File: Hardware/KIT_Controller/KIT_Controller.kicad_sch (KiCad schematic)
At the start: 1 part

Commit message: Satisfy constraints
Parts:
- added C1: 4.7uf, Capacitor_SMD:C_0805_2012Metric, symbol Device:C_Small
- added JP1: SolderJumper_2_Open, Jumper:SolderJumper-2_P1.3mm_Open_TrianglePad1.0x1.5mm, symbol Jumper:SolderJumper_2_Open
- gave numbers to parts that had none: 1
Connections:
- net at U1.2 (VOUT): now also C1.1
- net GND: now reaches U1.3 (GND)
- net GND: now also C1.2
- net at U1.4 (OSC): now also JP1.1 (A)
- net +3.3V: now reaches U1.9 (VCC)
- net +3.3V: now also JP1.2 (B)
- no-connect marks 0 -> 5
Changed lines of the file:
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@@
 (kicad_sch (version 20211123) (generator eeschema)
   (paper "A4")
+  (junction (at 224.79 114.3) (diameter 0) (color 0 0 0 0)
+  )
+  (junction (at 226.06 76.2) (diameter 0) (color 0 0 0 0)
+  )
+  (no_connect (at 212.09 97.155))
+  (no_connect (at 212.09 92.075))
+  (no_connect (at 212.09 94.615))
+  (no_connect (at 212.09 88.265))
+  (no_connect (at 212.09 99.695))
+  (wire (pts (xy 221.615 76.2) (xy 226.06 76.2))
+    (stroke (width 0) (type default) (color 0 0 0 0))
+  )
+  (wire (pts (xy 212.09 84.455) (xy 209.55 84.455))
+    (stroke (width 0) (type default) (color 0 0 0 0))
+  )
+  (wire (pts (xy 209.55 76.2) (xy 213.995 76.2))
+    (stroke (width 0) (type default) (color 0 0 0 0))
+  )
+  (wire (pts (xy 226.06 76.2) (xy 226.06 76.835))
+    (stroke (width 0) (type default) (color 0 0 0 0))
+  )
+  (wire (pts (xy 209.55 84.455) (xy 209.55 76.2))
+    (stroke (width 0) (type default) (color 0 0 0 0))
+  )
+  (wire (pts (xy 227.33 107.315) (xy 227.33 108.585))
+    (stroke (width 0) (type default) (color 0 0 0 0))
+  )
+  (wire (pts (xy 226.06 74.93) (xy 226.06 76.2))
+    (stroke (width 0) (type default) (color 0 0 0 0))
+  )
+  (wire (pts (xy 227.33 114.3) (xy 224.79 114.3))
+    (stroke (width 0) (type default) (color 0 0 0 0))
+  )
+  (wire (pts (xy 224.79 114.3) (xy 224.79 116.205))
+    (stroke (width 0) (type default) (color 0 0 0 0))
+  )
+  (wire (pts (xy 224.79 107.315) (xy 224.79 114.3))
+    (stroke (width 0) (type default) (color 0 0 0 0))
+  )
+  (wire (pts (xy 227.33 113.665) (xy 227.33 114.3))
+    (stroke (width 0) (type default) (color 0 0 0 0))
+  )
+  (symbol (lib_id "Jumper:SolderJumper_2_Open") (at 217.805 76.2 0) (unit 1)
+    (in_bom yes) (on_board yes)
+    (property "Reference" "JP1" (id 0) (at 217.805 73.66 0))
+    (property "Value" "SolderJumper_2_Open" (id 1) (at 217.805 72.39 0)
+      (effects (font (size 1.27 1.27)) hide)
+    )
+    (property "Footprint" "Jumper:SolderJumper-2_P1.3mm_Open_TrianglePad1.0x1.5mm" (id 2) (at 217.805 76.2 0)
+      (effects (font (size 1.27 1.27)) hide)
+    )
+    (property "Datasheet" "~" (id 3) (at 217.805 76.2 0)
+      (effects (font (size 1.27 1.27)) hide)
+    )
+    (pin "1")
+    (pin "2")
+  )
+  (symbol (lib_id "power:+3.3V") (at 226.06 74.93 0) (unit 1)
+    (in_bom yes) (on_board yes) (fields_autoplaced)
+    (property "Reference" "#PWR02" (id 0) (at 226.06 78.74 0)
+      (effects (font (size 1.27 1.27)) hide)
+    )
+    (property "Value" "+3.3V" (id 1) (at 226.06 69.85 0))
+    (property "Footprint" "" (id 2) (at 226.06 74.93 0)
+      (effects (font (size 1.27 1.27)) hide)
+    )
+    (property "Datasheet" "" (id 3) (at 226.06 74.93 0)
+      (effects (font (size 1.27 1.27)) hide)
+    )
+    (pin "1")
+  )
+  (symbol (lib_id "power:PWR_FLAG") (at 224.79 114.3 90) (unit 1)
+    (in_bom yes) (on_board yes) (fields_autoplaced)
+    (property "Reference" "#FLG0101" (id 0) (at 222.885 114.3 0)
+      (effects (font (size 1.27 1.27)) hide)
+    )
+    (property "Value" "PWR_FLAG" (id 1) (at 223.52 110.49 90))
+    (property "Footprint" "" (id 2) (at 224.79 114.3 0)
+      (effects (font (size 1.27 1.27)) hide)
+    )
+    (property "Datasheet" "~" (id 3) (at 224.79 114.3 0)
+      (effects (font (size 1.27 1.27)) hide)
+    )
+    (pin "1")
+  )
   (symbol (lib_id "nokia_5110-3310_lcd:Nokia_5110_LCD") (at 223.52 93.345 0) (unit 1)
     (in_bom yes) (on_board yes) (fields_autoplaced)
-    (property "Reference" "U?" (id 0) (at 231.14 90.805 0)
+    (property "Reference" "U1" (id 0) (at 231.14 90.805 0)
       (effects (font (size 1.524 1.524)) (justify left))
     )
@@
     (pin "9")
   )
+  (symbol (lib_id "Device:C_Small") (at 227.33 111.125 0) (unit 1)
+    (in_bom yes) (on_board yes) (fields_autoplaced)
+    (property "Reference" "C1" (id 0) (at 230.505 109.8612 0)
+      (effects (font (size 1.27 1.27)) (justify left))
+    )
+    (property "Value" "4.7uf" (id 1) (at 230.505 112.4012 0)
+      (effects (font (size 1.27 1.27)) (justify left))
+    )
+    (property "Footprint" "Capacitor_SMD:C_0805_2012Metric" (id 2) (at 227.33 111.125 0)
+      (effects (font (size 1.27 1.27)) hide)
+    )
+    (property "Datasheet" "~" (id 3) (at 227.33 111.125 0)
+      (effects (font (size 1.27 1.27)) hide)
+    )
+    (pin "1")
+    (pin "2")
+  )
+  (symbol (lib_id "power:GND") (at 224.79 116.205 0) (unit 1)
+    (in_bom yes) (on_board yes) (fields_autoplaced)
+    (property "Reference" "#PWR01" (id 0) (at 224.79 122.555 0)
+      (effects (font (size 1.27 1.27)) hide)
+    )
+    (property "Value" "GND" (id 1) (at 224.79 121.285 0))
+    (property "Footprint" "" (id 2) (at 224.79 116.205 0)
+      (effects (font (size 1.27 1.27)) hide)
+    )
+    (property "Datasheet" "" (id 3) (at 224.79 116.205 0)
+      (effects (font (size 1.27 1.27)) hide)
+    )
+    (pin "1")
+  )
+  (symbol (lib_id "power:PWR_FLAG") (at 226.06 76.2 270) (unit 1)
+    (in_bom yes) (on_board yes) (fields_autoplaced)
+    (property "Reference" "#FLG0102" (id 0) (at 227.965 76.2 0)
+      (effects (font (size 1.27 1.27)) hide)
+    )
+    (property "Value" "PWR_FLAG" (id 1) (at 229.87 76.1999 90)
+      (effects (font (size 1.27 1.27)) (justify left))
+    )
+    (property "Footprint" "" (id 2) (at 226.06 76.2 0)
+      (effects (font (size 1.27 1.27)) hide)
+    )
+    (property "Datasheet" "~" (id 3) (at 226.06 76.2 0)
+      (effects (font (size 1.27 1.27)) hide)
+    )
+    (pin "1")
+  )
   (sheet_instances
     (path "/" (page "1"))
   )
   (symbol_instances
+    (path "/4eb8585d-c31d-4b73-92b2-292a151f185e"
+      (reference "#FLG0101") (unit 1) (value "PWR_FLAG") (footprint "")
+    )
+    (path "/ecdf7f93-19b9-4617-b0cd-e32253294f59"
+      (reference "#FLG0102") (unit 1) (value "PWR_FLAG") (footprint "")
+    )
+    (path "/846a239b-d6fe-40f8-ba97-eca7b90437c7"
+      (reference "#PWR01") (unit 1) (value "GND") (footprint "")
+    )
+    (path "/13f49aed-0c42-4453-bcb8-cd4e227fdfb5"
+      (reference "#PWR02") (unit 1) (value "+3.3V") (footprint "")
+    )
+    (path "/6ab78924-1dc0-46f4-aacc-52e33f151645"
+      (reference "C1") (unit 1) (value "4.7uf") (footprint "Capacitor_SMD:C_0805_2012Metric")
+    )
+    (path "/034c73e5-9967-4b8a-b103-11b25b0768f1"
+      (reference "JP1") (unit 1) (value "SolderJumper_2_Open") (footprint "Jumper:SolderJumper-2_P1.3mm_Open_TrianglePad1.0x1.5mm")
+    )
     (path "/623154dc-1575-4b27-b483-8c3196e0409b"
-      (reference "U?") (unit 1) (value "Nokia_5110_LCD") (footprint "Nokia_5110-3310_LCD:Nokia_5110-3310_LCD")
+      (reference "U1") (unit 1) (value "Nokia_5110_LCD") (footprint "Nokia_5110-3310_LCD:Nokia_5110-3310_LCD")
     )
   )

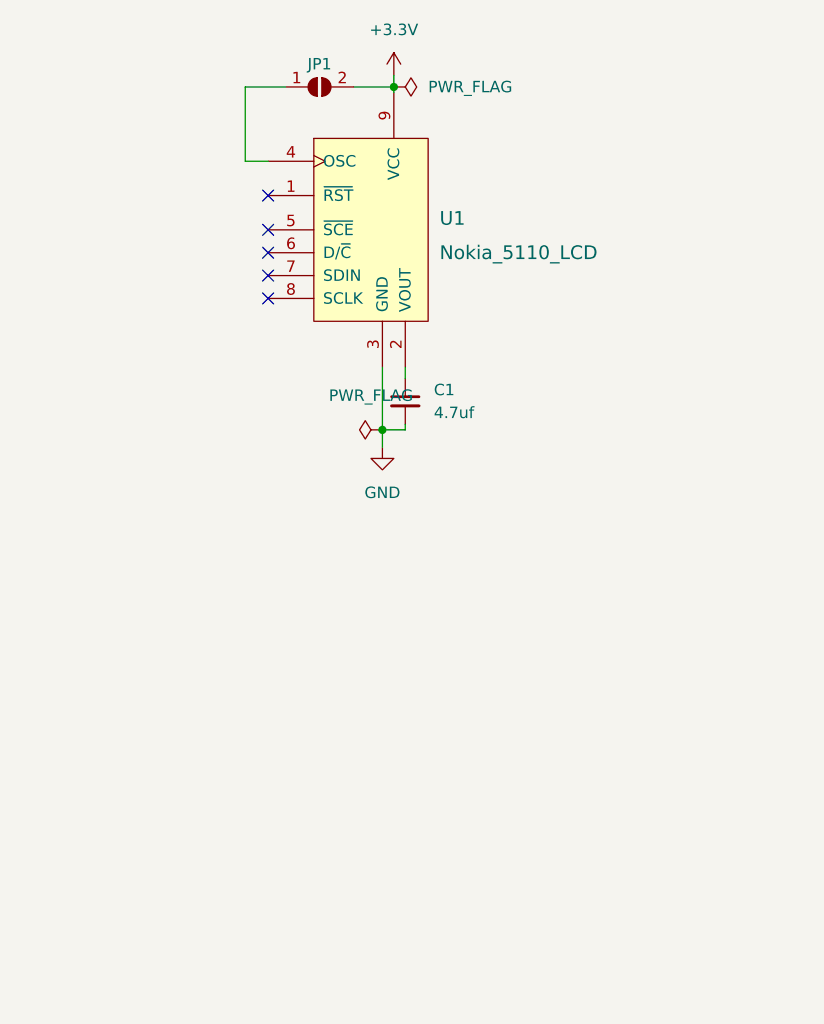
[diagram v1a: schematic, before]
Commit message: Cleanup external libs and add extra bits to brd
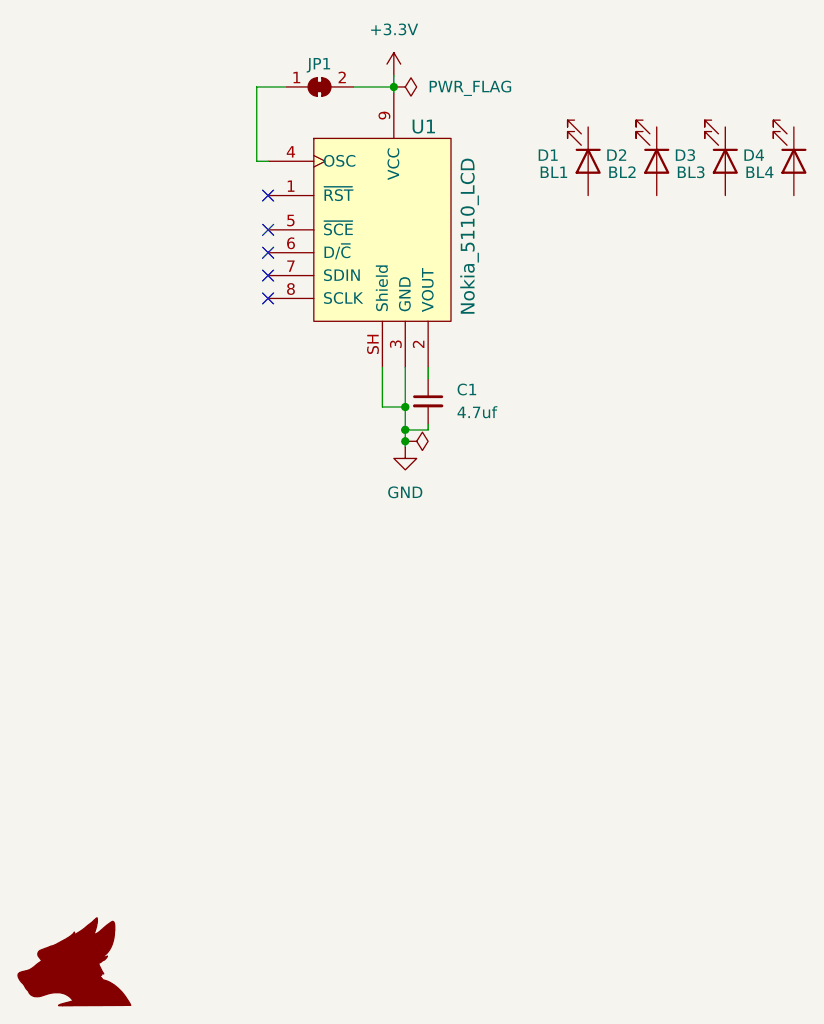
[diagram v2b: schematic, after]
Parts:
- removed JP1: SolderJumper_2_Open, Jumper:SolderJumper-2_P1.3mm_Open_TrianglePad1.0x1.5mm, symbol Jumper:SolderJumper_2_Open
- added D1: BL1, LED_SMD:LED_0805_2012Metric, symbol Device:LED
- added D2: BL2, LED_SMD:LED_0805_2012Metric, symbol Device:LED
- added D3: BL3, LED_SMD:LED_0805_2012Metric, symbol Device:LED
- added D4: BL4, LED_SMD:LED_0805_2012Metric, symbol Device:LED
- added JP1: SolderJumper_2_Bridged, Jumper:SolderJumper-2_P1.3mm_Bridged_Pad1.0x1.5mm, symbol Jumper:SolderJumper_2_Bridged
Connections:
- net +3.3V: now also JP1.2 (B)
- net GND: now also U1.SH (Shield)
- net at U1.4 (OSC): now also JP1.1 (A)
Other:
- company: (none) -> Kitsune Scientific
- title: (none) -> KIT Mainboard
- moved on the sheet: C1

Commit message: Pad more components
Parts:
- added C101, C102: 27p, Capacitor_SMD:C_0805_2012Metric, symbol Device:C_Small
- added C103, C113: 1u, Capacitor_SMD:C_0805_2012Metric, symbol Device:C_Small
- added C104, C105, C106, C107, C108, C109, C110, C111, C112: 100n, Capacitor_SMD:C_0805_2012Metric, symbol Device:C_Small
- added R101: 1k, Resistor_SMD:R_0805_2012Metric, symbol Device:R_Small
- added R102, R103: 27, Resistor_SMD:R_0805_2012Metric, symbol Device:R_Small
- added U101: RP2040, Package_DFN_QFN:QFN-56-1EP_7x7mm_P0.4mm_EP3.2x3.2mm_ThermalVias, symbol KenwoodFox:RP2040
- added Y101: Crystal, Crystal:Crystal_SMD_HC49-SD, symbol Device:Crystal
- renumbered C1 to C114, D1 to D101, D2 to D102, D3 to D103, D4 to D104, JP1 to JP101, U1 to U102
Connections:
- net GND: now also C101.1, C102.1, C103.1, C104.1, C105.1, C106.1, C107.1, C108.1, C109.1, C110.1, C111.1, C112.1, C113.1, U101.19 (TESTEN), U101.57 (GND)
- net +3.3V renamed +3V3
- net +3V3: now also C106.2, C107.2, C108.2, C109.2, C110.2, C111.2, C112.2, C113.2, U101.1 (IOVDD), U101.10 (IOVDD), U101.22 (IOVDD), U101.33 (IOVDD), U101.42 (IOVDD), U101.43 (ADC_AVDD), U101.44 (VREG_IN), U101.48 (USB_VDD), U101.49 (IOVDD)
- new net: R103.1, U101.46 (USB_DM)
- new net: R102.1, U101.47 (USB_DP)
- new net: C102.2, R101.1, Y101.1
- new net +1V1: C103.2, C104.2, C105.2, U101.23 (DVDD), U101.45 (VREG_VOUT), U101.50 (DVDD)
- new net USB_D+: R102.2
- new net USB_D-: R103.2
- new net XIN: C101.2, U101.20 (XIN), Y101.2
- new net XOUT: R101.2, U101.21 (XOUT)
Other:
- note added: "ABLS-12.000MHZ-B4-T"
- note added: "Place 1u as close to pin 10 as possible"
- note added: "Place 1u as close to pin 45 as possible"

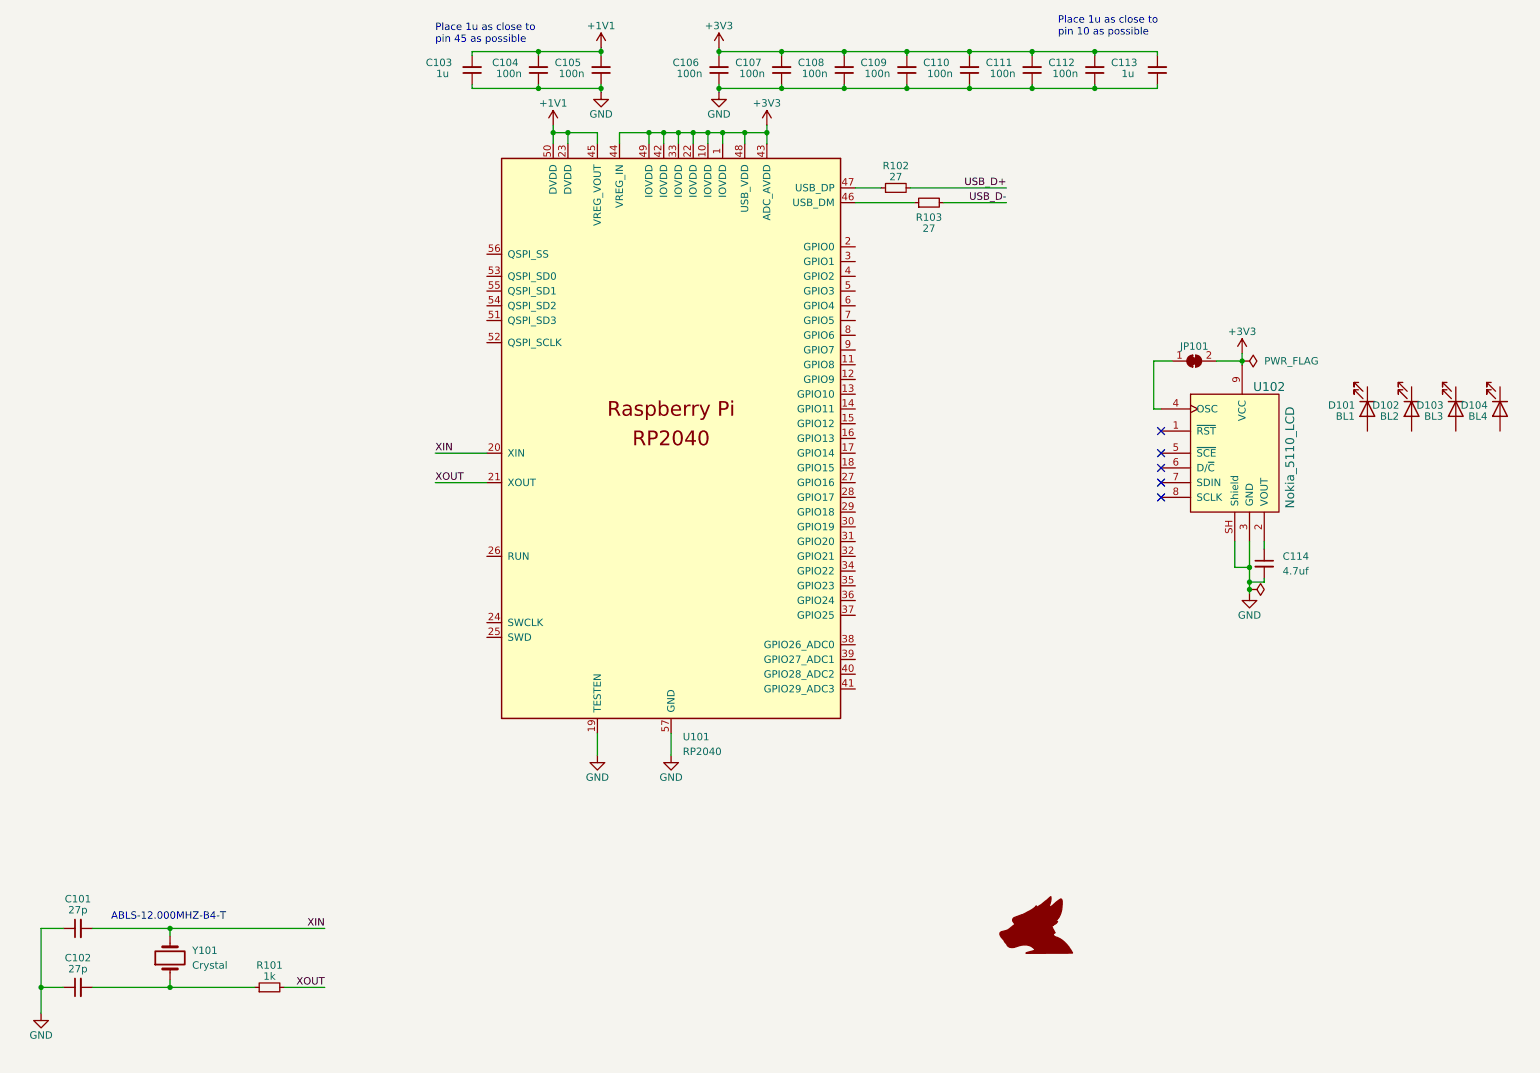
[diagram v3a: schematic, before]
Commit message: Move MCU to its own schem
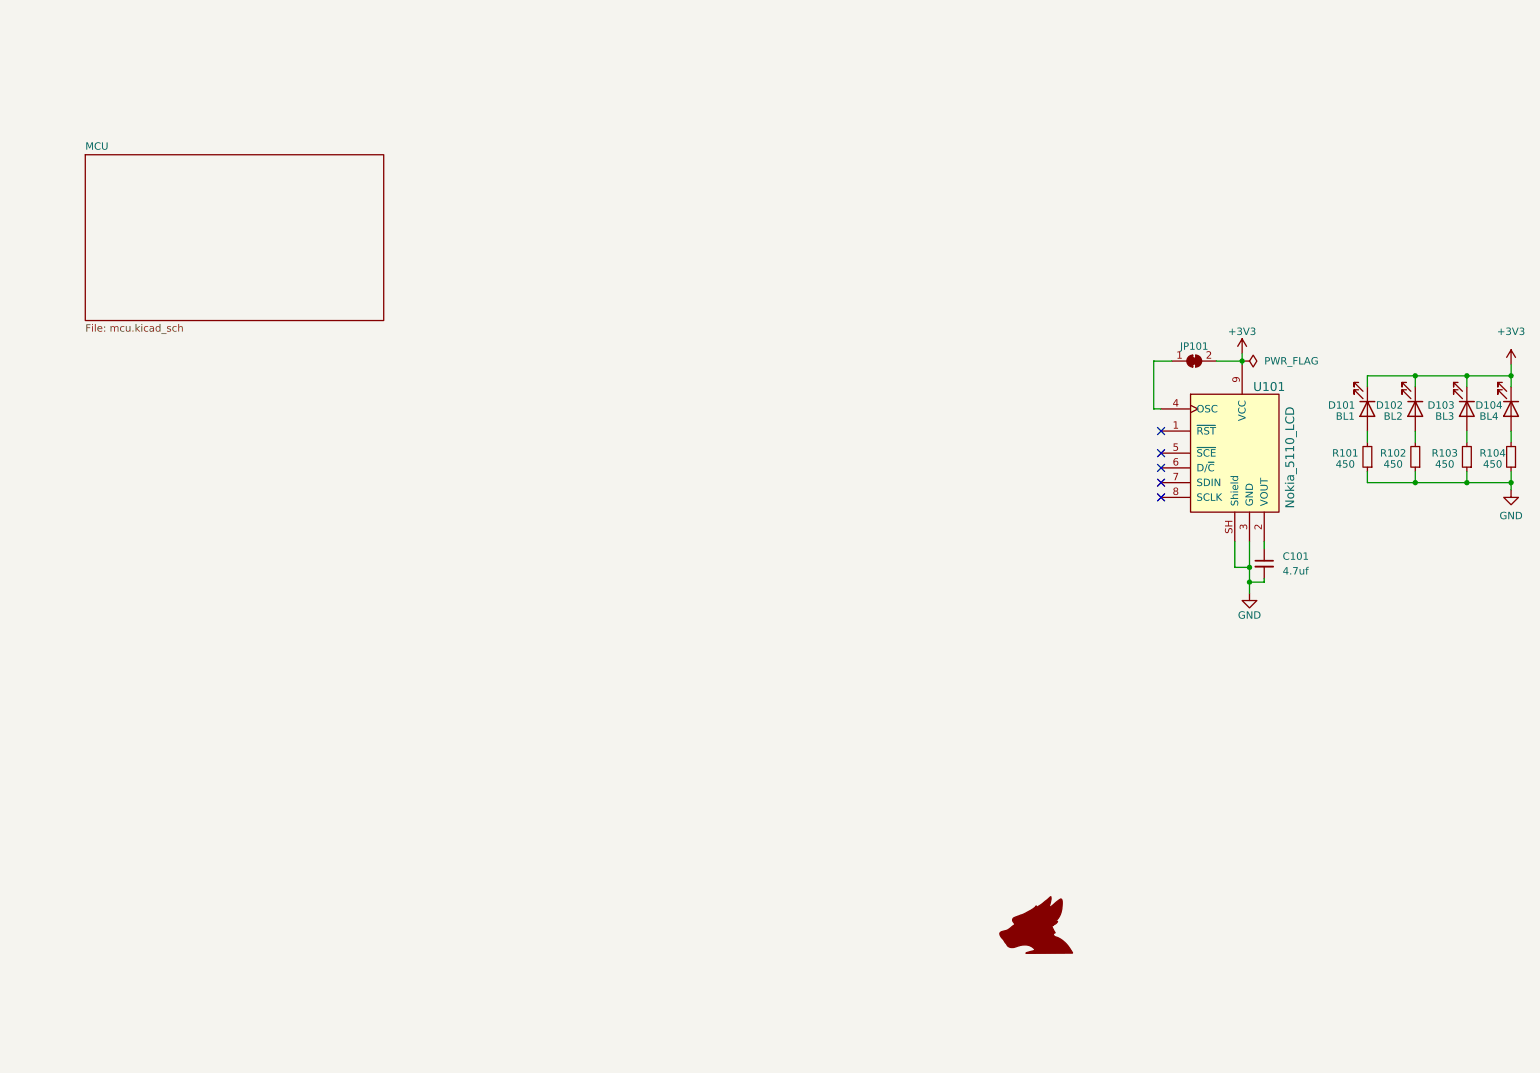
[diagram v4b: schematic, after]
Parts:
- removed C101, C102: 27p, Capacitor_SMD:C_0805_2012Metric, symbol Device:C_Small
- removed C103, C113: 1u, Capacitor_SMD:C_0805_2012Metric, symbol Device:C_Small
- removed C104, C105, C106, C107, C108, C109, C110, C111, C112: 100n, Capacitor_SMD:C_0805_2012Metric, symbol Device:C_Small
- removed U101: RP2040, Package_DFN_QFN:QFN-56-1EP_7x7mm_P0.4mm_EP3.2x3.2mm_ThermalVias, symbol KenwoodFox:RP2040
- removed Y101: Crystal, Crystal:Crystal_SMD_HC49-SD, symbol Device:Crystal
- added R104: 450, Resistor_SMD:R_0805_2012Metric, symbol Device:R_Small
- R101: value 1k -> 450
- R102, R103: value 27 -> 450
- renumbered C114 to C101, U102 to U101
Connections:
- net USB_D+ is gone; now on an unnamed net: R102.2
- net USB_D- is gone; now on an unnamed net: R103.2
- net XOUT is gone; now on an unnamed net: R101.2
- net +3V3: now also D101.1 (K), D102.1 (K), D103.1 (K), D104.1 (K)
- net GND: now also R101.1, R102.1, R103.1, R104.1
- net at D104.2 (A): now also R104.2
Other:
- added sheet MCU (mcu.kicad_sch)
- note removed: "ABLS-12.000MHZ-B4-T"
- note removed: "Place 1u as close to pin 10 as possible"
- note removed: "Place 1u as close to pin 45 as possible"
- moved on the sheet: D102, D103, D104
